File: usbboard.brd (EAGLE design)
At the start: 12 x 6.5 mm, 2 parts

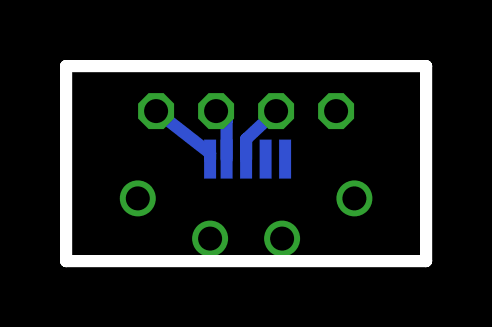
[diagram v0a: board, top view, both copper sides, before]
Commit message: fixed intial board errors, including short, flipped usb, and missing trace
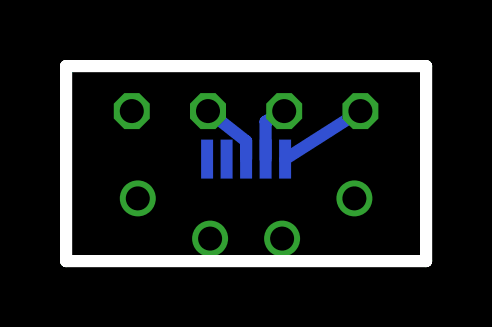
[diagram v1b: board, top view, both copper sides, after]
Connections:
- net D+: now also U$3.2; no longer U$3.3
- net D-: now also U$3.3; no longer U$3.2
- net GND: now also U$3.1; no longer U$3.4
- net USB+: now also U$3.4; no longer U$3.1
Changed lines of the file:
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@@
 <contactref element="MICRO-USB" pad="GND3"/>
 <contactref element="MICRO-USB" pad="GND2"/>
-<contactref element="U$3" pad="4"/>
 <contactref element="MICRO-USB" pad="GND"/>
 <polygon width="0.254" layer="1" thermals="no">
@@
 <vertex x="38.5" y="40"/>
 </polygon>
+<contactref element="U$3" pad="1"/>
 </signal>
 <signal name="D+">
-<contactref element="U$3" pad="3"/>
 <contactref element="MICRO-USB" pad="D+"/>
-<wire x1="32.5" y1="43.4" x2="32.5" y2="44.065" width="0.4064" layer="16"/>
-<wire x1="32.5" y1="44.065" x2="33.5" y2="45" width="0.4064" layer="16"/>
+<contactref element="U$3" pad="2"/>
+<wire x1="32.5" y1="43.4" x2="32.5" y2="44" width="0.4064" layer="16"/>
+<wire x1="32.5" y1="44" x2="31.23" y2="45" width="0.4064" layer="16"/>
 </signal>
 <signal name="D-">
-<contactref element="U$3" pad="2"/>
 <contactref element="MICRO-USB" pad="D-"/>
-<wire x1="31.85" y1="43.4" x2="31.85" y2="44.685" width="0.4064" layer="16"/>
-<wire x1="31.85" y1="44.685" x2="31.5" y2="45" width="0.4064" layer="16"/>
+<contactref element="U$3" pad="3"/>
+<wire x1="33.15" y1="43.4" x2="33.15" y2="44.65" width="0.4064" layer="16"/>
+<wire x1="33.15" y1="44.65" x2="33.77" y2="45" width="0.4064" layer="16"/>
 </signal>
 <signal name="USB+">
-<contactref element="U$3" pad="1"/>
 <contactref element="MICRO-USB" pad="VCC"/>
-<wire x1="31.3" y1="43.4" x2="31.3" y2="43.595" width="0.4064" layer="16"/>
-<wire x1="31.3" y1="43.595" x2="29.5" y2="45" width="0.4064" layer="16"/>
+<contactref element="U$3" pad="4"/>
+<wire x1="33.8" y1="43.4" x2="36.31" y2="45" width="0.4064" layer="16"/>
 </signal>
 </signals>

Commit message: fixed collision issue
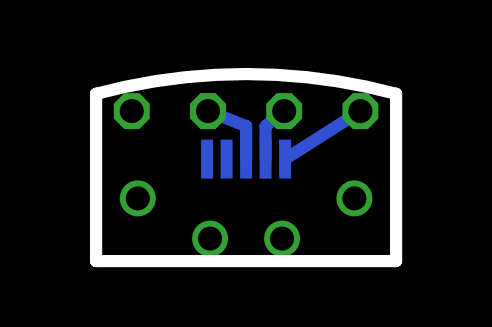
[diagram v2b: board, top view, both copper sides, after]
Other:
- board size 12 x 6.5 mm -> 10 x 6.2 mm
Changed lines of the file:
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@@
 <board>
 <plain>
-<wire x1="26.5" y1="40" x2="38.5" y2="40" width="0.4064" layer="20"/>
-<wire x1="26.5" y1="40" x2="26.5" y2="46.5" width="0.4064" layer="20"/>
-<wire x1="38.5" y1="40" x2="38.5" y2="46.5" width="0.4064" layer="20"/>
-<wire x1="26.5" y1="46.5" x2="38.5" y2="46.5" width="0.4064" layer="20"/>
+<wire x1="27.5" y1="40" x2="37.5" y2="40" width="0.4064" layer="20"/>
+<wire x1="27.5" y1="40" x2="27.5" y2="45.576696875" width="0.4064" layer="20"/>
+<wire x1="37.5" y1="40" x2="37.5" y2="45.576696875" width="0.4064" layer="20"/>
+<wire x1="27.5" y1="45.576696875" x2="37.5" y2="45.576696875" width="0.4064" layer="20" curve="-30"/>
 </plain>
 <attributes>
@@
 <contactref element="MICRO-USB" pad="GND"/>
 <polygon width="0.254" layer="1" thermals="no">
-<vertex x="26.5" y="46.5"/>
-<vertex x="26.5" y="40"/>
-<vertex x="38.5" y="40"/>
-<vertex x="38.5" y="46.5"/>
+<vertex x="27.5" y="45.576696875"/>
+<vertex x="27.5" y="40"/>
+<vertex x="37.5" y="40"/>
+<vertex x="37.5" y="45.576696875" curve="30"/>
 </polygon>
 <polygon width="0.254" layer="16" thermals="no">
-<vertex x="26.5" y="40"/>
-<vertex x="26.5" y="46.5"/>
-<vertex x="38.5" y="46.5"/>
-<vertex x="38.5" y="40"/>
+<vertex x="27.5" y="40"/>
+<vertex x="27.5" y="45.576696875" curve="-30"/>
+<vertex x="37.5" y="45.576696875"/>
+<vertex x="37.5" y="40"/>
 </polygon>
 <contactref element="U$3" pad="1"/>
@@
 <contactref element="MICRO-USB" pad="D+"/>
 <contactref element="U$3" pad="2"/>
-<wire x1="32.5" y1="43.4" x2="32.5" y2="44" width="0.4064" layer="16"/>
-<wire x1="32.5" y1="44" x2="31.23" y2="45" width="0.4064" layer="16"/>
+<wire x1="32.5" y1="43.4" x2="32.5" y2="44.5" width="0.4064" layer="16"/>
+<wire x1="32.5" y1="44.5" x2="31.23" y2="45" width="0.4064" layer="16"/>
 </signal>
 <signal name="D-">
 <contactref element="MICRO-USB" pad="D-"/>
 <contactref element="U$3" pad="3"/>
-<wire x1="33.15" y1="43.4" x2="33.15" y2="44.65" width="0.4064" layer="16"/>
-<wire x1="33.15" y1="44.65" x2="33.77" y2="45" width="0.4064" layer="16"/>
+<wire x1="33.15" y1="43.4" x2="33.15" y2="44.5" width="0.4064" layer="16"/>
+<wire x1="33.15" y1="44.5" x2="33.77" y2="45" width="0.4064" layer="16"/>
 </signal>
 <signal name="USB+">
